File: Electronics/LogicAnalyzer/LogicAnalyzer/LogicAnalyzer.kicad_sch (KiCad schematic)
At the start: 6 parts, among them J1 Conn_02x15_Odd_Even, J2 Conn_01x03, J3 Conn_01x03, U1 Pico

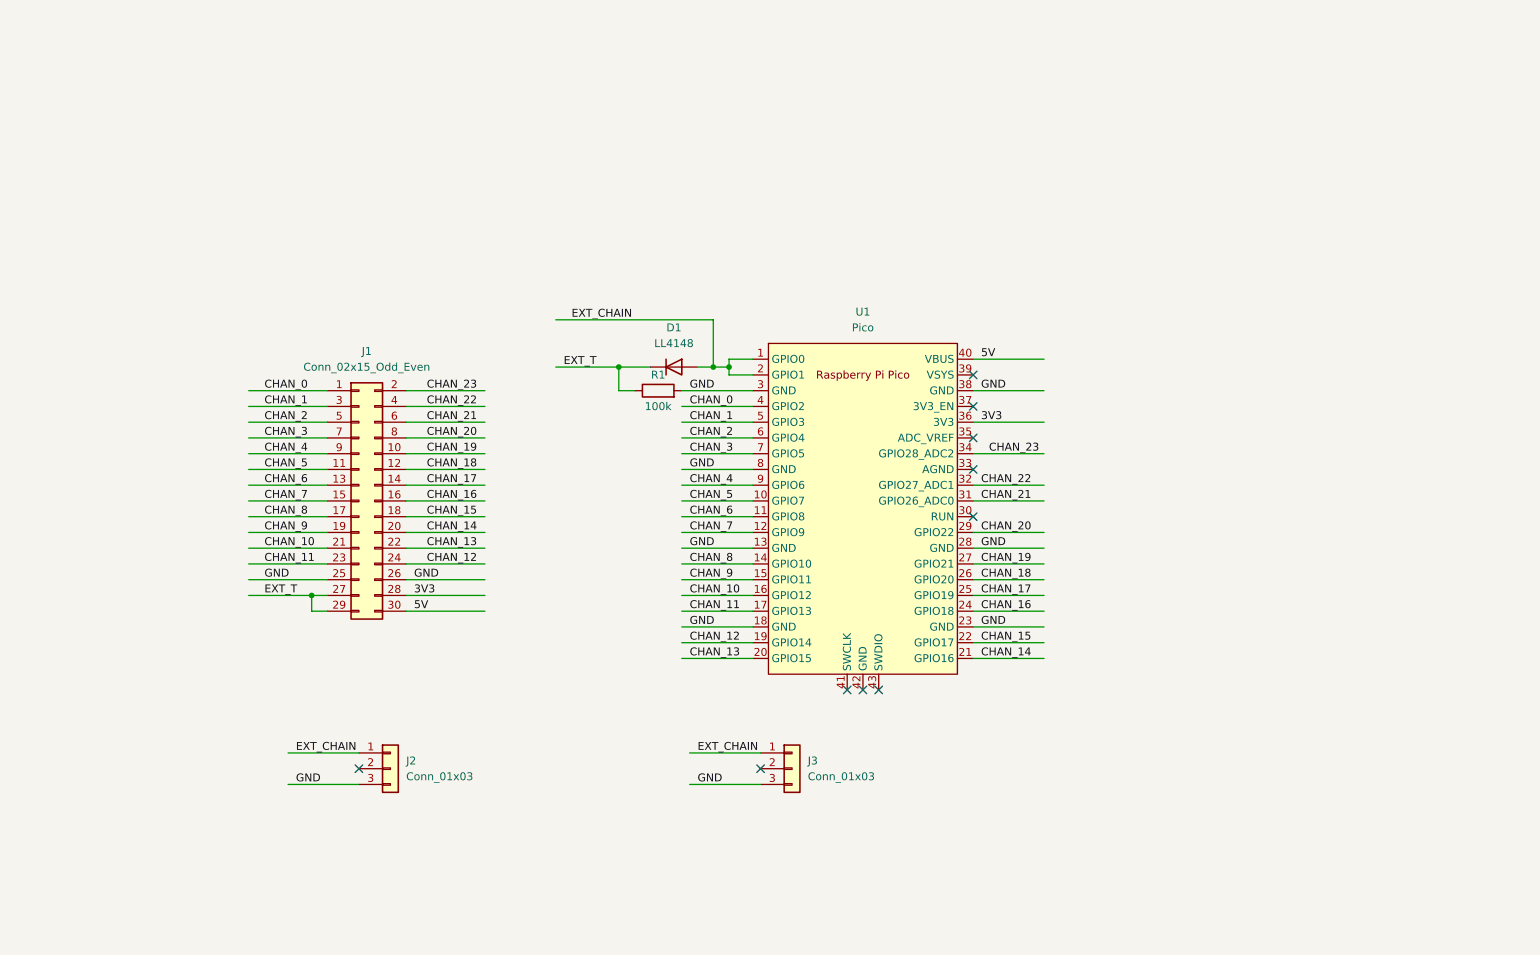
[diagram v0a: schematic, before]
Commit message: Version 5.0 of PCB
- Integrated bidirectional voltage translators
- Added Power LED
- Switchable internal or external reference voltage
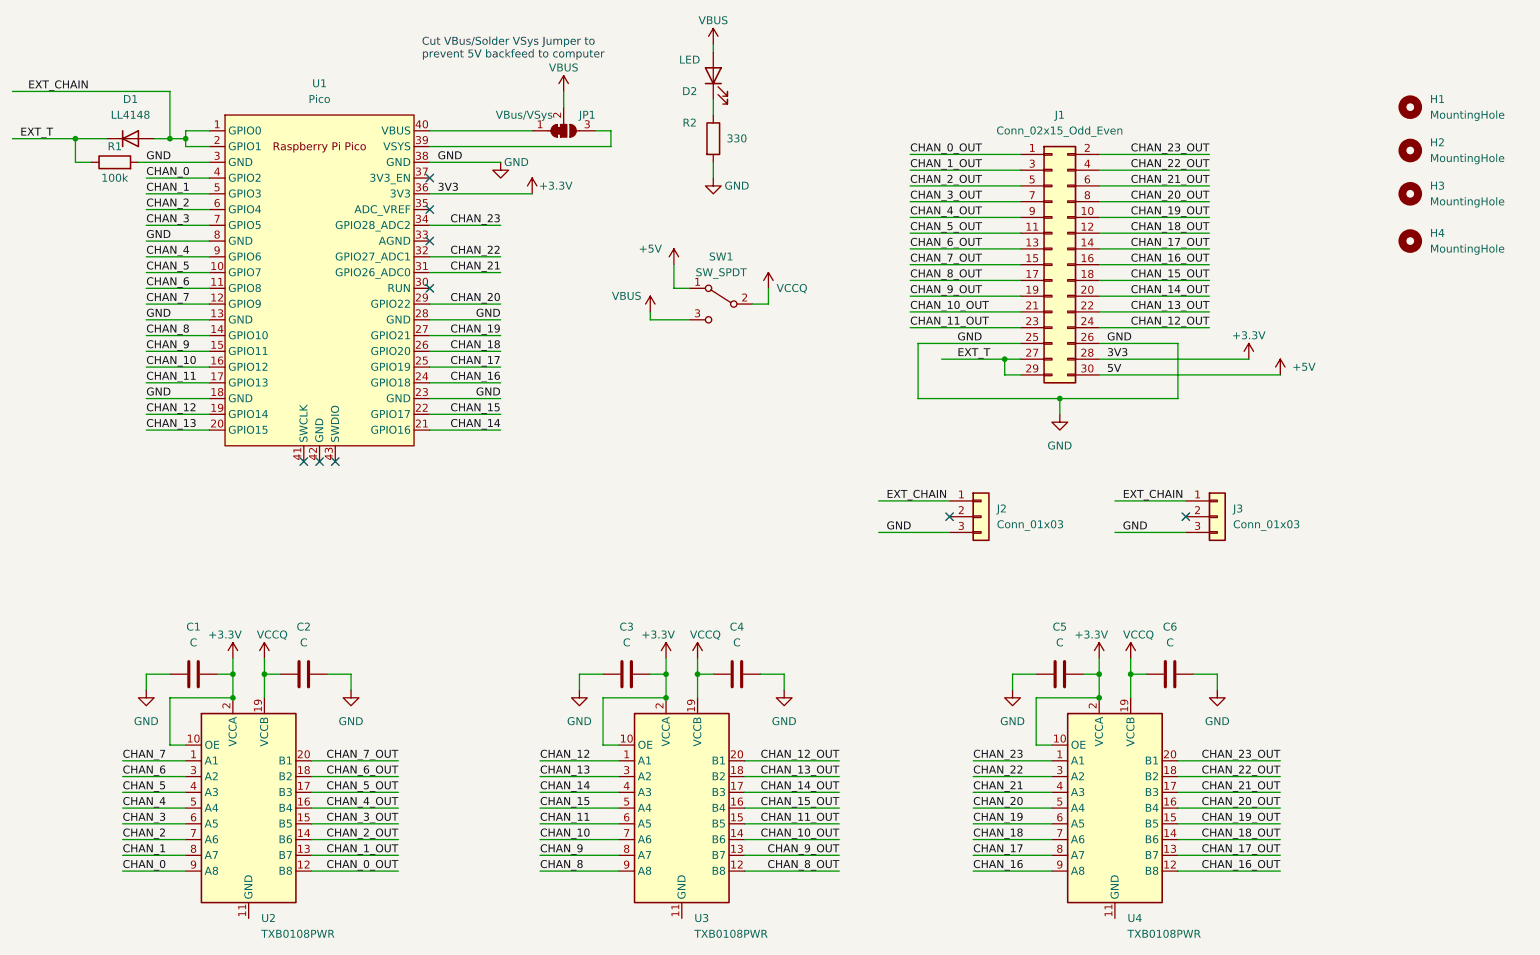
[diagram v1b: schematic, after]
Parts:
- added C1, C2, C3, C4, C5, C6: C, Capacitor_SMD:C_0805_2012Metric, symbol Device:C
- added D2: LED, LED_SMD:LED_1206_3216Metric, symbol Device:LED
- added H1, H2, H3, H4: MountingHole, MountingHole:MountingHole_3.2mm_M3_DIN965_Pad_TopBottom, symbol Mechanical:MountingHole
- added JP1: VBus/VSys, Jumper:SolderJumper-3_P1.3mm_Bridged12_RoundedPad1.0x1.5mm, symbol Jumper:SolderJumper_3_Bridged12
- added R2: 330, Resistor_SMD:R_0805_2012Metric, symbol Device:R
- added SW1: SW_SPDT, Button_Switch_SMD:SW_SPDT_PCM12, symbol Switch:SW_SPDT
- added U2, U3, U4: TXB0108PWR, Package_SO:TSSOP-20_4.4x6.5mm_P0.65mm, symbol Logic_LevelTranslator:TXB0108PWR
- D1: footprint Diode_SMD:D_MiniMELF -> Diode_SMD:D_SMA
- R1: footprint Resistor_SMD:R_0603_1608Metric -> Resistor_SMD:R_0805_2012Metric
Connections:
- net CHAN_0: now also U2.9 (A8); no longer J1.1 (Pin_1)
- net CHAN_1: now also U2.8 (A7); no longer J1.3 (Pin_3)
- net CHAN_10: now also U3.7 (A6); no longer J1.21 (Pin_21)
- net CHAN_11: now also U3.6 (A5); no longer J1.23 (Pin_23)
- net CHAN_12: now also U3.1 (A1); no longer J1.24 (Pin_24)
- net CHAN_13: now also U3.3 (A2); no longer J1.22 (Pin_22)
- net CHAN_14: now also U3.4 (A3); no longer J1.20 (Pin_20)
- net CHAN_15: now also U3.5 (A4); no longer J1.18 (Pin_18)
- net CHAN_16: now also U4.9 (A8); no longer J1.16 (Pin_16)
- net CHAN_17: now also U4.8 (A7); no longer J1.14 (Pin_14)
- net CHAN_18: now also U4.7 (A6); no longer J1.12 (Pin_12)
- net CHAN_19: now also U4.6 (A5); no longer J1.10 (Pin_10)
- net CHAN_2: now also U2.7 (A6); no longer J1.5 (Pin_5)
- net CHAN_20: now also U4.5 (A4); no longer J1.8 (Pin_8)
- net CHAN_21: now also U4.4 (A3); no longer J1.6 (Pin_6)
- net CHAN_22: now also U4.3 (A2); no longer J1.4 (Pin_4)
- net CHAN_23: now also U4.1 (A1); no longer J1.2 (Pin_2)
- net CHAN_3: now also U2.6 (A5); no longer J1.7 (Pin_7)
- net CHAN_4: now also U2.5 (A4); no longer J1.9 (Pin_9)
- net CHAN_5: now also U2.4 (A3); no longer J1.11 (Pin_11)
- net CHAN_6: now also U2.3 (A2); no longer J1.13 (Pin_13)
- net CHAN_7: now also U2.1 (A1); no longer J1.15 (Pin_15)
- net CHAN_8: now also U3.9 (A8); no longer J1.17 (Pin_17)
- net CHAN_9: now also U3.8 (A7); no longer J1.19 (Pin_19)
- net GND: now also C1.1, C2.2, C3.1, C4.2, C5.1, C6.2, R2.2
- net at U1.39 (VSYS): now also JP1.3 (B)
- net 3V3 renamed +3.3V
- net +3.3V: now also C1.2, C3.2, C5.2, U2.10 (OE), U2.2 (VCCA), U3.10 (OE), U3.2 (VCCA), U4.10 (OE), U4.2 (VCCA)
- net 5V: no longer names the net of U1.40 (VBUS)
- net 5V: now also JP1.1 (A); no longer J1.30 (Pin_30)
- new net: D2.1 (K), R2.1
- new net +5V: J1.30 (Pin_30), SW1.1 (A)
- new net CHAN_0_OUT: J1.1 (Pin_1), U2.12 (B8)
- new net CHAN_10_OUT: J1.21 (Pin_21), U3.14 (B6)
- new net CHAN_11_OUT: J1.23 (Pin_23), U3.15 (B5)
- new net CHAN_12_OUT: J1.24 (Pin_24), U3.20 (B1)
- new net CHAN_13_OUT: J1.22 (Pin_22), U3.18 (B2)
- new net CHAN_14_OUT: J1.20 (Pin_20), U3.17 (B3)
- new net CHAN_15_OUT: J1.18 (Pin_18), U3.16 (B4)
- new net CHAN_16_OUT: J1.16 (Pin_16), U4.12 (B8)
- new net CHAN_17_OUT: J1.14 (Pin_14), U4.13 (B7)
- new net CHAN_18_OUT: J1.12 (Pin_12), U4.14 (B6)
- new net CHAN_19_OUT: J1.10 (Pin_10), U4.15 (B5)
- new net CHAN_1_OUT: J1.3 (Pin_3), U2.13 (B7)
- new net CHAN_20_OUT: J1.8 (Pin_8), U4.16 (B4)
- new net CHAN_21_OUT: J1.6 (Pin_6), U4.17 (B3)
- new net CHAN_22_OUT: J1.4 (Pin_4), U4.18 (B2)
- new net CHAN_23_OUT: J1.2 (Pin_2), U4.20 (B1)
- new net CHAN_2_OUT: J1.5 (Pin_5), U2.14 (B6)
- new net CHAN_3_OUT: J1.7 (Pin_7), U2.15 (B5)
- new net CHAN_4_OUT: J1.9 (Pin_9), U2.16 (B4)
- new net CHAN_5_OUT: J1.11 (Pin_11), U2.17 (B3)
- new net CHAN_6_OUT: J1.13 (Pin_13), U2.18 (B2)
- new net CHAN_7_OUT: J1.15 (Pin_15), U2.20 (B1)
- new net CHAN_8_OUT: J1.17 (Pin_17), U3.12 (B8)
- new net CHAN_9_OUT: J1.19 (Pin_19), U3.13 (B7)
- new net VBUS: D2.2 (A), JP1.2 (C), SW1.3 (C)
- new net VCCQ: C2.1, C4.1, C6.1, SW1.2 (B), U2.19 (VCCB), U3.19 (VCCB), U4.19 (VCCB)
- no-connect marks 10 -> 9
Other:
- note added: "Cut VBus/Solder VSys Jumper to prevent 5V backfeed to computer"
- moved on the sheet: D1, J1, J2, J3, R1, U1
